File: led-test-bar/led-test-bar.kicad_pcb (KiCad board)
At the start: 2 copper layers, 174 x 16.5 mm, 33 parts, among them J1 Conn_01x31_Male

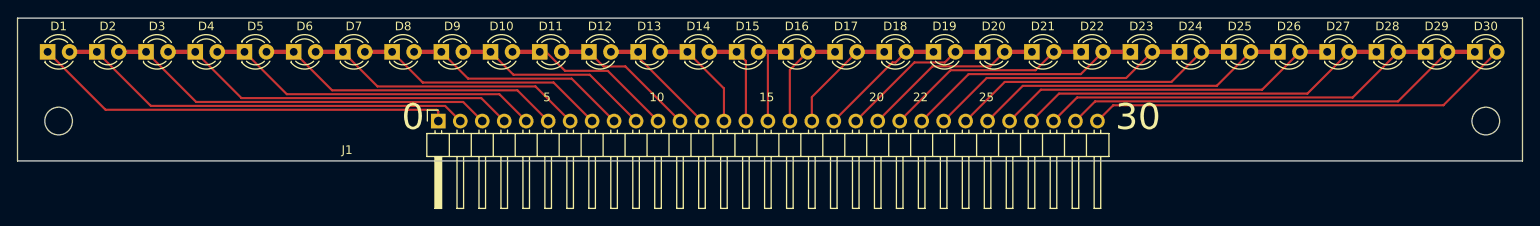
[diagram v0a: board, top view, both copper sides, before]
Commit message: Copper pours, and some clippable pads for the lowest voltage.
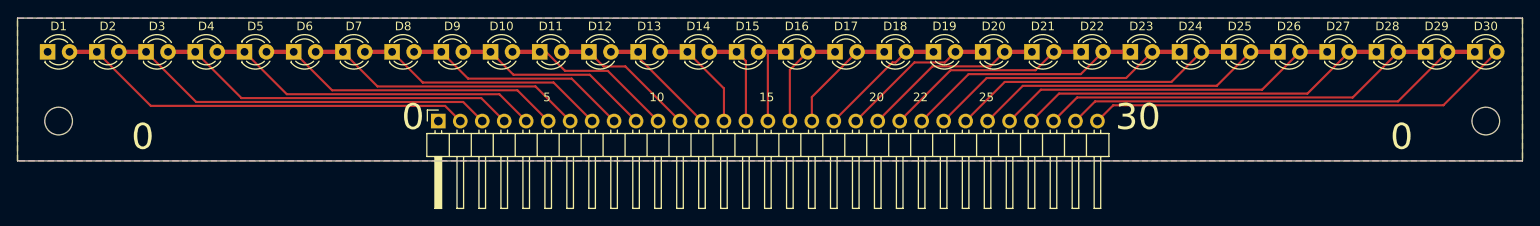
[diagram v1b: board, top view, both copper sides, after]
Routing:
- net Net-(D1-Pad1): track 49.1 -> 0.00 mm
- added copper zone on B.Cu, net Net-(D1-Pad1)
- added copper zone on F.Cu, net Net-(D1-Pad1)

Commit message: Add/update board rev silkscreen, nothing else
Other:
- board text added: "http://github.com/jkominek/piano-conversion LED test bar Rev0"
